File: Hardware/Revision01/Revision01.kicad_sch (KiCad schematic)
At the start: 23 parts, among them J1 Battery connector, SW2 SW_SPST_LED, U10 NCP1117LPST50T3G

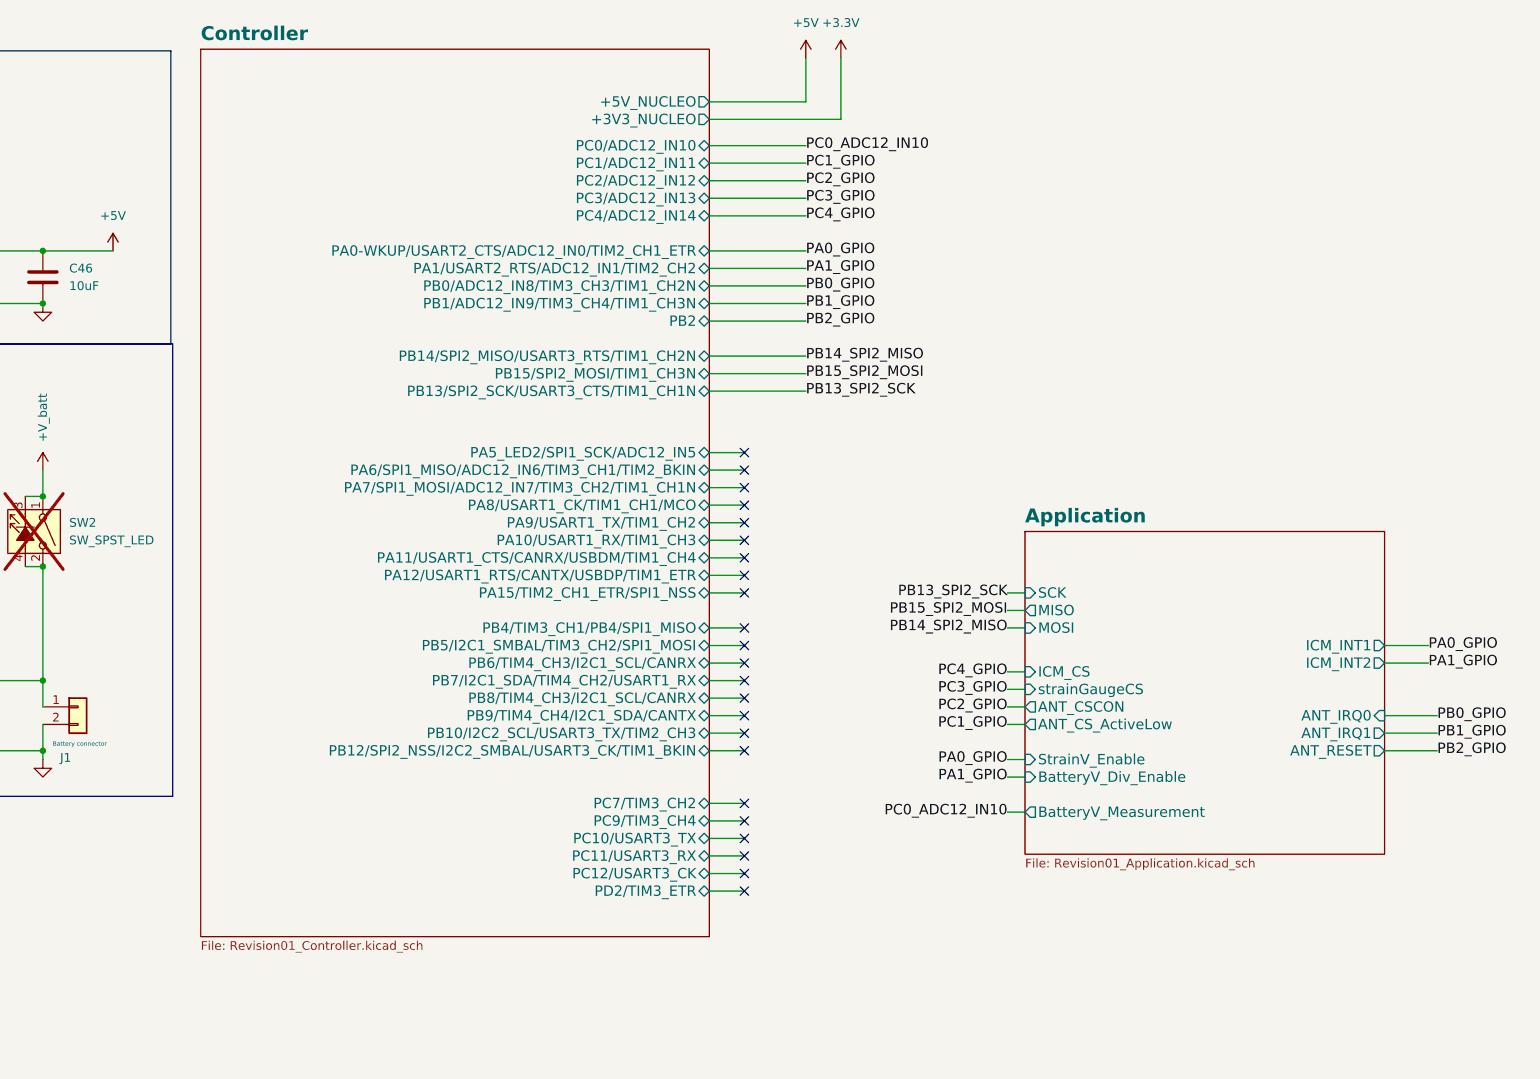
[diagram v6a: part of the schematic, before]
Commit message: Reworked Controller sheet to nucleo L476RG
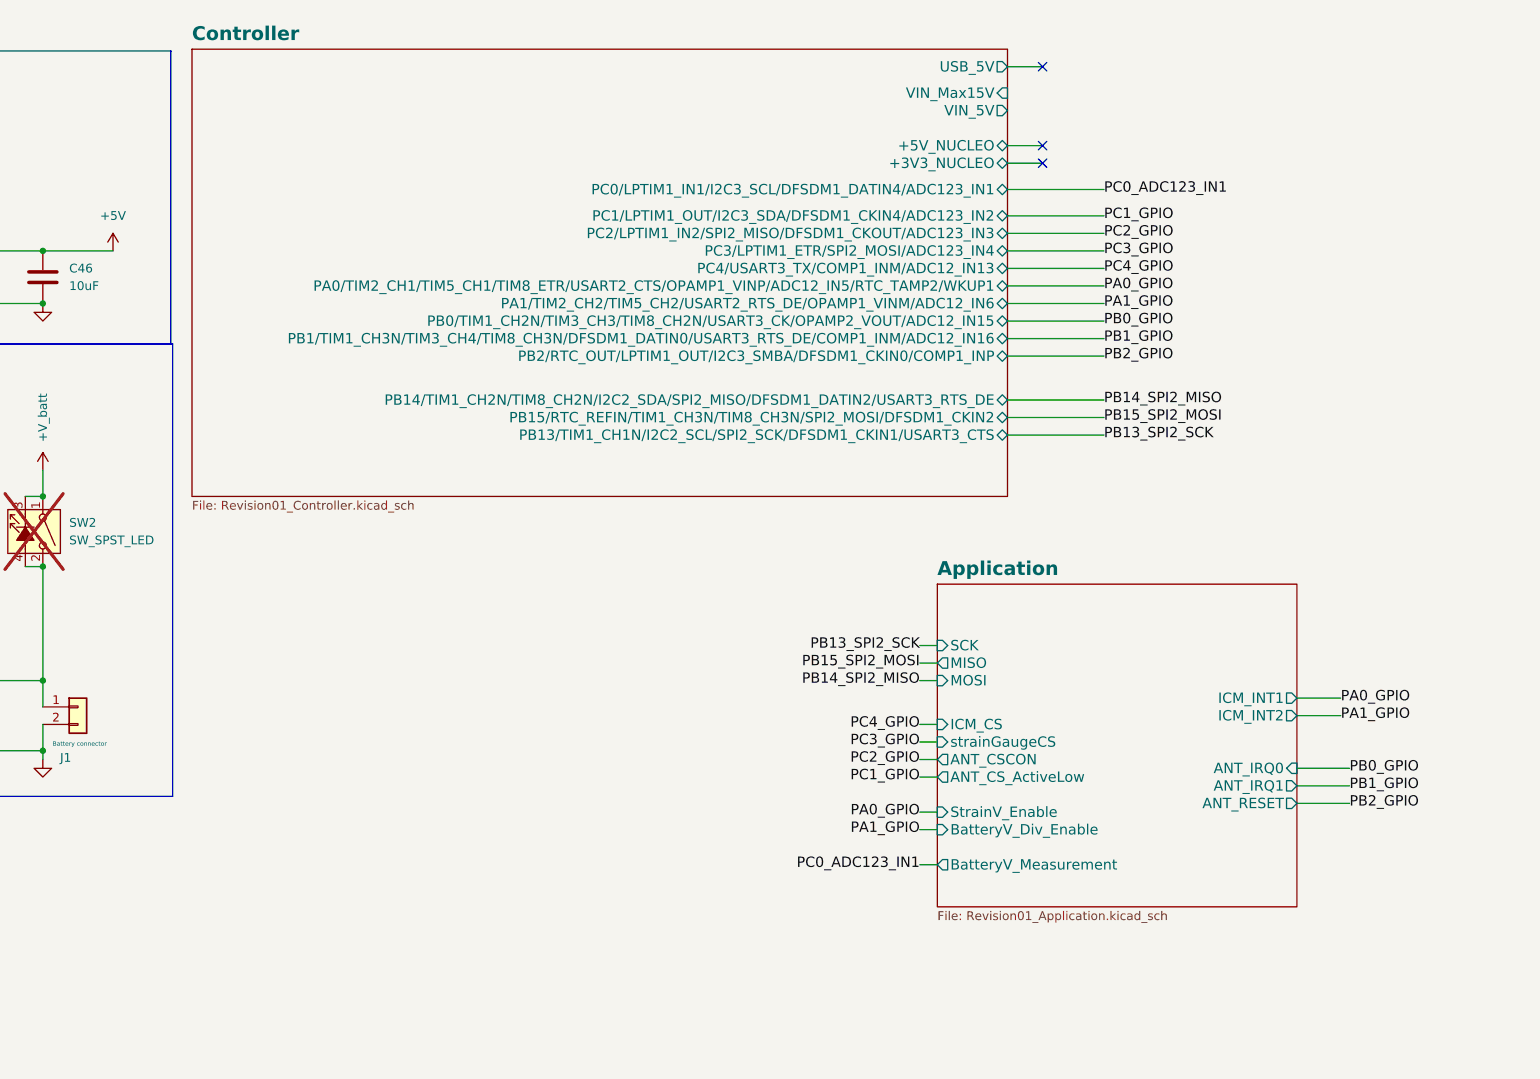
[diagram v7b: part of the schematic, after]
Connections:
- no-connect marks 24 -> 4
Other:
- sheet Controller ports: added PA0/TIM2_CH1/TIM5_CH1/TIM8_ETR/USART2_CTS/OPAMP1_VINP/ADC12_IN5/RTC_TAMP2/WKUP1, PA1/TIM2_CH2/TIM5_CH2/USART2_RTS_DE/OPAMP1_VINM/ADC12_IN6, PB0/TIM1_CH2N/TIM3_CH3/TIM8_CH2N/USART3_CK/OPAMP2_VOUT/ADC12_IN15, PB1/TIM1_CH3N/TIM3_CH4/TIM8_CH3N/DFSDM1_DATIN0/USART3_RTS_DE/COMP1_INM/ADC12_IN16, PB13/TIM1_CH1N/I2C2_SCL/SPI2_SCK/DFSDM1_CKIN1/USART3_CTS, PB14/TIM1_CH2N/TIM8_CH2N/I2C2_SDA/SPI2_MISO/DFSDM1_DATIN2/USART3_RTS_DE, PB15/RTC_REFIN/TIM1_CH3N/TIM8_CH3N/SPI2_MOSI/DFSDM1_CKIN2, PB2/RTC_OUT/LPTIM1_OUT/I2C3_SMBA/DFSDM1_CKIN0/COMP1_INP, PC0/LPTIM1_IN1/I2C3_SCL/DFSDM1_DATIN4/ADC123_IN1, PC1/LPTIM1_OUT/I2C3_SDA/DFSDM1_CKIN4/ADC123_IN2, PC2/LPTIM1_IN2/SPI2_MISO/DFSDM1_CKOUT/ADC123_IN3, PC3/LPTIM1_ETR/SPI2_MOSI/ADC123_IN4, PC4/USART3_TX/COMP1_INM/ADC12_IN13, USB_5V, VIN_5V, VIN_Max15V; removed PA0-WKUP/USART2_CTS/ADC12_IN0/TIM2_CH1_ETR, PA10/USART1_RX/TIM1_CH3, PA11/USART1_CTS/CANRX/USBDM/TIM1_CH4, PA12/USART1_RTS/CANTX/USBDP/TIM1_ETR, PA15/TIM2_CH1_ETR/SPI1_NSS, PA1/USART2_RTS/ADC12_IN1/TIM2_CH2, PA5_LED2/SPI1_SCK/ADC12_IN5, PA6/SPI1_MISO/ADC12_IN6/TIM3_CH1/TIM2_BKIN, PA7/SPI1_MOSI/ADC12_IN7/TIM3_CH2/TIM1_CH1N, PA8/USART1_CK/TIM1_CH1/MCO, PA9/USART1_TX/TIM1_CH2, PB0/ADC12_IN8/TIM3_CH3/TIM1_CH2N, PB10/I2C2_SCL/USART3_TX/TIM2_CH3, PB12/SPI2_NSS/I2C2_SMBAL/USART3_CK/TIM1_BKIN, PB13/SPI2_SCK/USART3_CTS/TIM1_CH1N, PB14/SPI2_MISO/USART3_RTS/TIM1_CH2N, PB15/SPI2_MOSI/TIM1_CH3N, PB1/ADC12_IN9/TIM3_CH4/TIM1_CH3N, PB2, PB4/TIM3_CH1/PB4/SPI1_MISO, PB5/I2C1_SMBAL/TIM3_CH2/SPI1_MOSI, PB6/TIM4_CH3/I2C1_SCL/CANRX, PB7/I2C1_SDA/TIM4_CH2/USART1_RX, PB8/TIM4_CH3/I2C1_SCL/CANRX, PB9/TIM4_CH4/I2C1_SDA/CANTX, PC0/ADC12_IN10, PC10/USART3_TX, PC11/USART3_RX, PC12/USART3_CK, PC1/ADC12_IN11, PC2/ADC12_IN12, PC3/ADC12_IN13, PC4/ADC12_IN14, PC7/TIM3_CH2, PC9/TIM3_CH4, PD2/TIM3_ETR

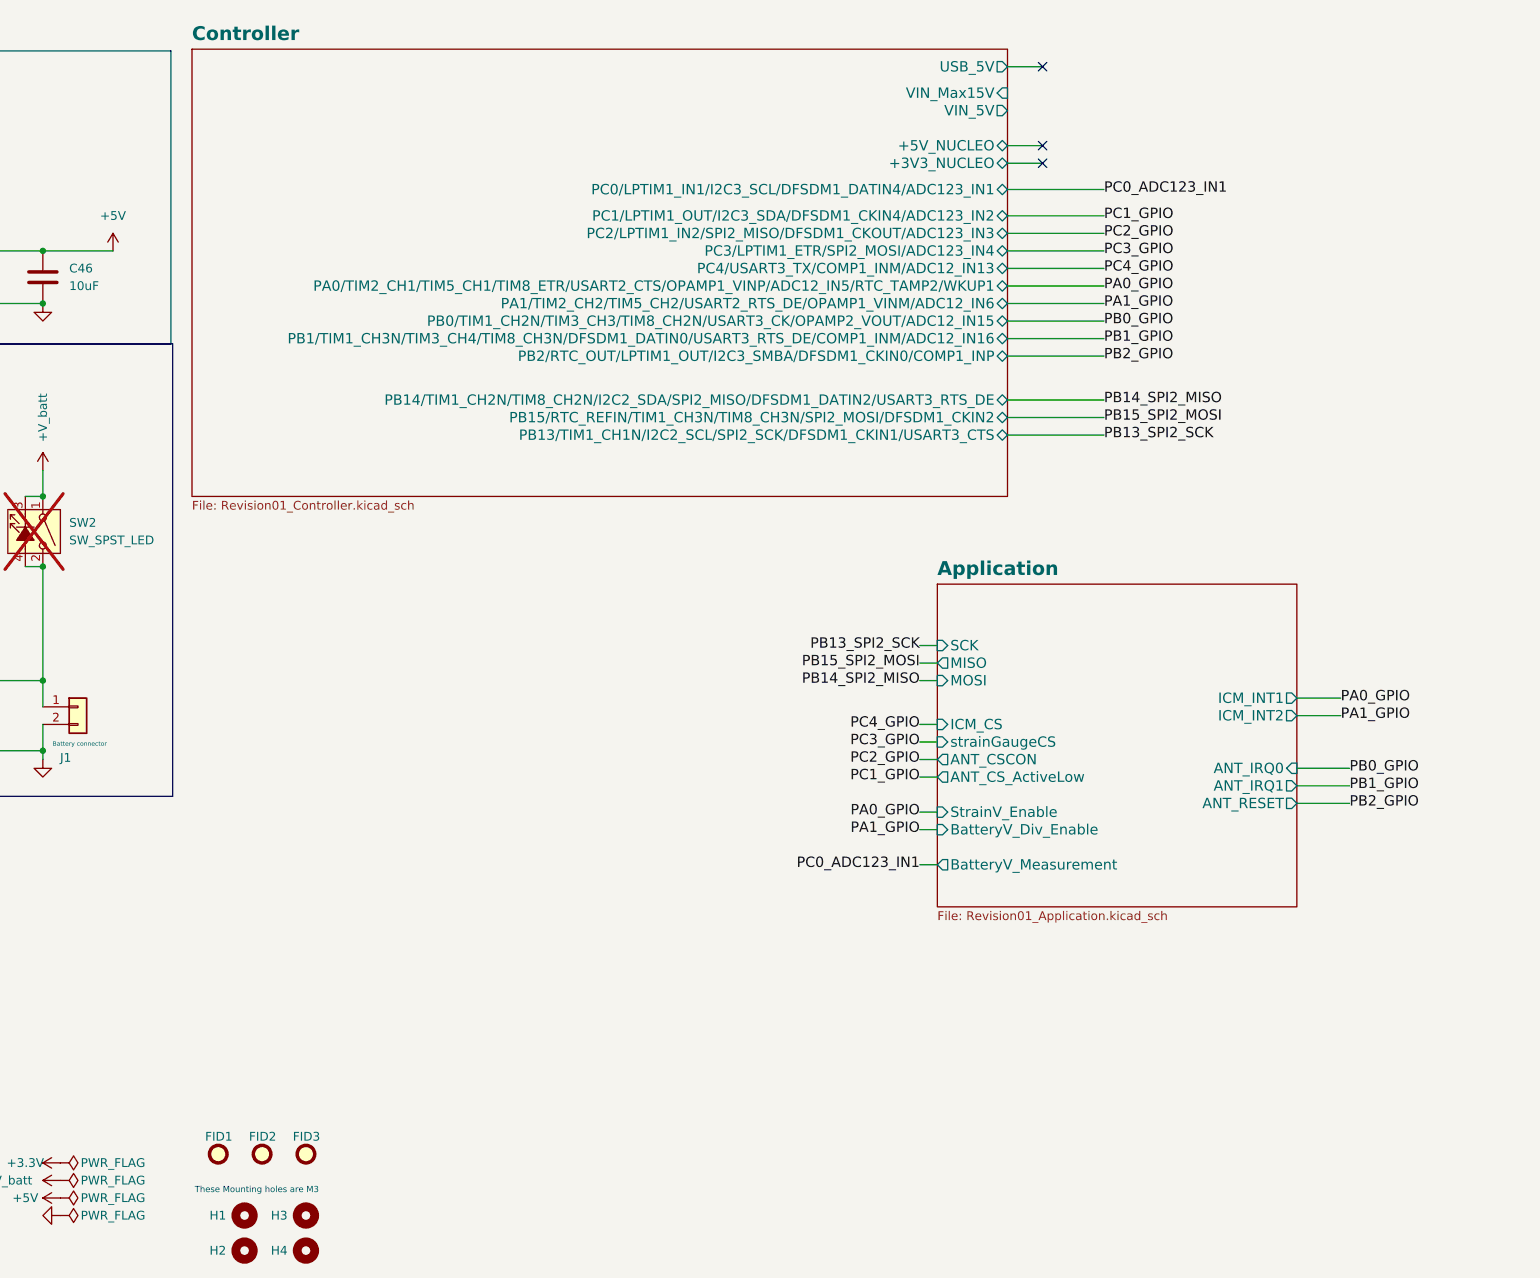
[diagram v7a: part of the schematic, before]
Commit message: ADDED 25pF to STRAIN GAUGES to remove noise ADDED FOOTPRINTS TO COMPONENTS Changed PS back to external-highside switch as internal mosfet current rating is too low pull-up for PMOS strainV_enable added Reconfigured new Nucleo board STM32IDE file
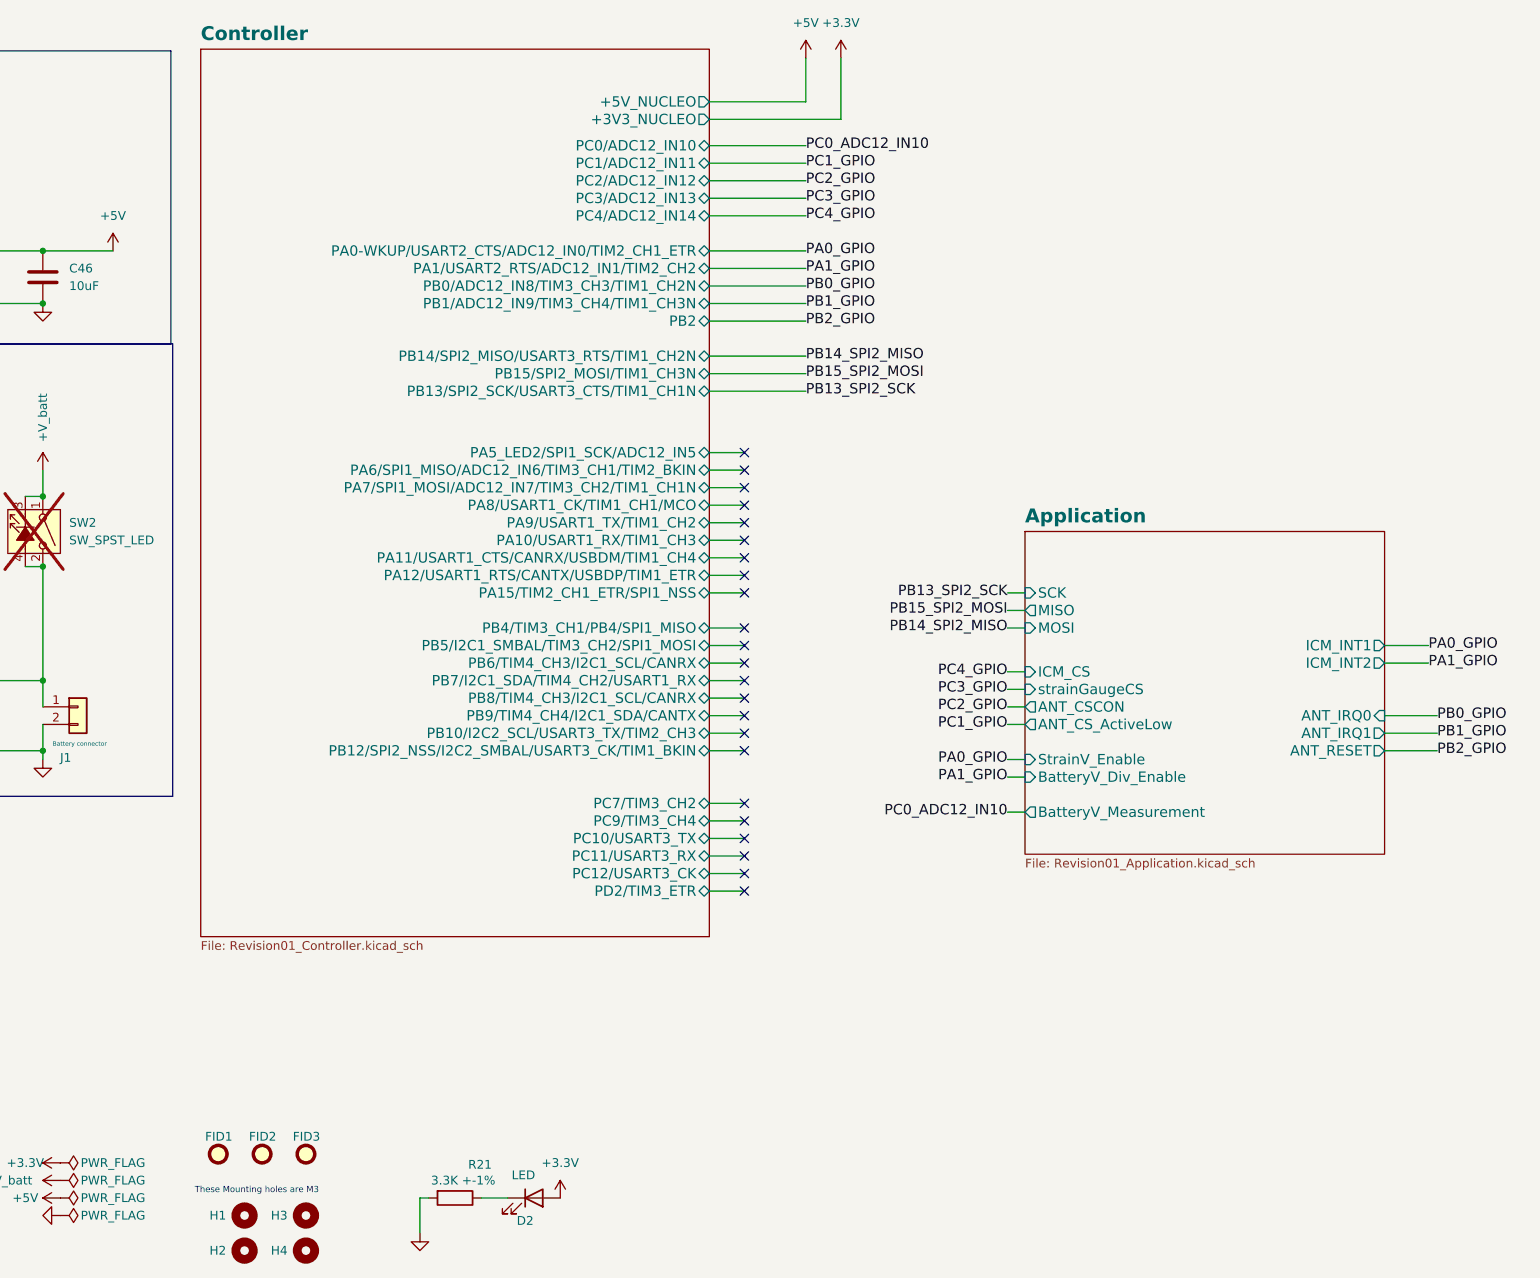
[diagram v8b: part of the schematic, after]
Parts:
- added D2: LED, LED_SMD:LED_0402_1005Metric, symbol Device:LED
- added R21: 3.3K +-1%, Resistor_SMD:R_0805_2012Metric, symbol Device:R
- TP1, TP2, TP3: footprint TestPoint:TestPoint_THTPad_1.0x1.0mm_Drill0.5mm -> TestPoint:TestPoint_Pad_2.0x2.0mm
- TP4, TP5, TP6: footprint TestPoint:TestPoint_THTPad_1.0x1.0mm_Drill0.5mm -> TestPoint:TestPoint_THTPad_2.5x2.5mm_Drill1.2mm
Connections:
- net +3.3V: now also D2.2 (A)
- net GND: now also R21.2
- new net: D2.1 (K), R21.1
- no-connect marks 4 -> 24
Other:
- sheet Controller ports: added PA0-WKUP/USART2_CTS/ADC12_IN0/TIM2_CH1_ETR, PA10/USART1_RX/TIM1_CH3, PA11/USART1_CTS/CANRX/USBDM/TIM1_CH4, PA12/USART1_RTS/CANTX/USBDP/TIM1_ETR, PA15/TIM2_CH1_ETR/SPI1_NSS, PA1/USART2_RTS/ADC12_IN1/TIM2_CH2, PA5_LED2/SPI1_SCK/ADC12_IN5, PA6/SPI1_MISO/ADC12_IN6/TIM3_CH1/TIM2_BKIN, PA7/SPI1_MOSI/ADC12_IN7/TIM3_CH2/TIM1_CH1N, PA8/USART1_CK/TIM1_CH1/MCO, PA9/USART1_TX/TIM1_CH2, PB0/ADC12_IN8/TIM3_CH3/TIM1_CH2N, PB10/I2C2_SCL/USART3_TX/TIM2_CH3, PB12/SPI2_NSS/I2C2_SMBAL/USART3_CK/TIM1_BKIN, PB13/SPI2_SCK/USART3_CTS/TIM1_CH1N, PB14/SPI2_MISO/USART3_RTS/TIM1_CH2N, PB15/SPI2_MOSI/TIM1_CH3N, PB1/ADC12_IN9/TIM3_CH4/TIM1_CH3N, PB2, PB4/TIM3_CH1/PB4/SPI1_MISO, PB5/I2C1_SMBAL/TIM3_CH2/SPI1_MOSI, PB6/TIM4_CH3/I2C1_SCL/CANRX, PB7/I2C1_SDA/TIM4_CH2/USART1_RX, PB8/TIM4_CH3/I2C1_SCL/CANRX, PB9/TIM4_CH4/I2C1_SDA/CANTX, PC0/ADC12_IN10, PC10/USART3_TX, PC11/USART3_RX, PC12/USART3_CK, PC1/ADC12_IN11, PC2/ADC12_IN12, PC3/ADC12_IN13, PC4/ADC12_IN14, PC7/TIM3_CH2, PC9/TIM3_CH4, PD2/TIM3_ETR; removed PA0/TIM2_CH1/TIM5_CH1/TIM8_ETR/USART2_CTS/OPAMP1_VINP/ADC12_IN5/RTC_TAMP2/WKUP1, PA1/TIM2_CH2/TIM5_CH2/USART2_RTS_DE/OPAMP1_VINM/ADC12_IN6, PB0/TIM1_CH2N/TIM3_CH3/TIM8_CH2N/USART3_CK/OPAMP2_VOUT/ADC12_IN15, PB1/TIM1_CH3N/TIM3_CH4/TIM8_CH3N/DFSDM1_DATIN0/USART3_RTS_DE/COMP1_INM/ADC12_IN16, PB13/TIM1_CH1N/I2C2_SCL/SPI2_SCK/DFSDM1_CKIN1/USART3_CTS, PB14/TIM1_CH2N/TIM8_CH2N/I2C2_SDA/SPI2_MISO/DFSDM1_DATIN2/USART3_RTS_DE, PB15/RTC_REFIN/TIM1_CH3N/TIM8_CH3N/SPI2_MOSI/DFSDM1_CKIN2, PB2/RTC_OUT/LPTIM1_OUT/I2C3_SMBA/DFSDM1_CKIN0/COMP1_INP, PC0/LPTIM1_IN1/I2C3_SCL/DFSDM1_DATIN4/ADC123_IN1, PC1/LPTIM1_OUT/I2C3_SDA/DFSDM1_CKIN4/ADC123_IN2, PC2/LPTIM1_IN2/SPI2_MISO/DFSDM1_CKOUT/ADC123_IN3, PC3/LPTIM1_ETR/SPI2_MOSI/ADC123_IN4, PC4/USART3_TX/COMP1_INM/ADC12_IN13, USB_5V, VIN_5V, VIN_Max15V
- title: sensor system -> TELEMETRY SYSTEM
